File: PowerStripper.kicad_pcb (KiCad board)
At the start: 4 copper layers, 42.7 x 38.3 mm, 5 parts, among them J1 0548190519, J2 UE27AC54100

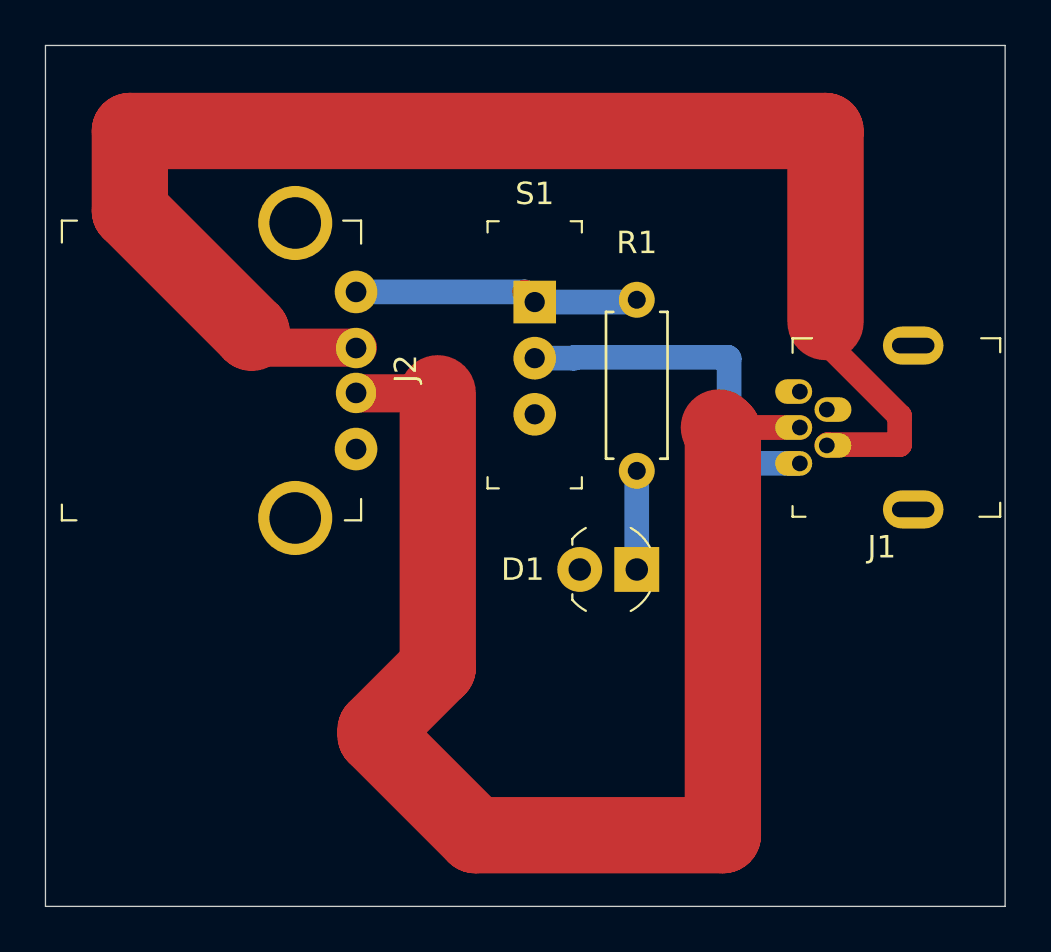
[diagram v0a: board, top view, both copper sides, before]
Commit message: finished making changes to make it compatible with jlcpcb
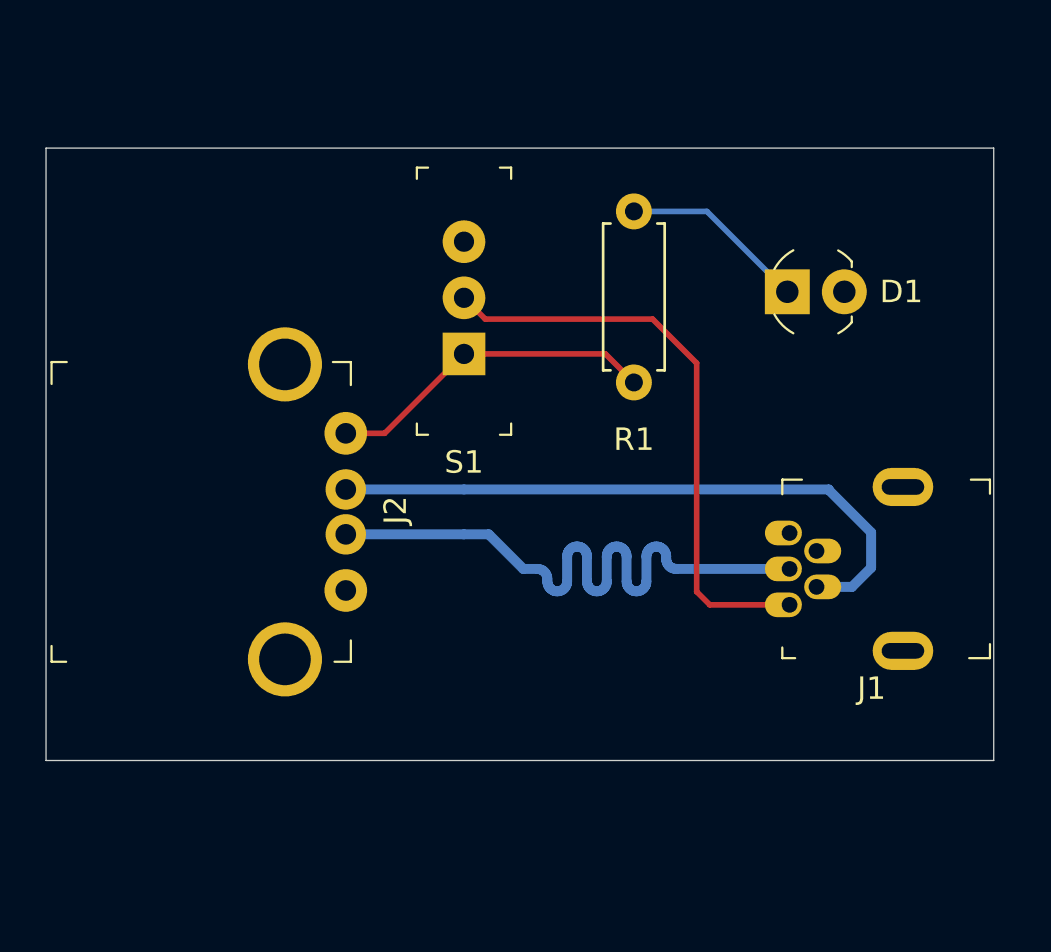
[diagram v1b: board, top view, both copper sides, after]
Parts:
- moved D1 17.1 mm to (128.1, 99.9), turned to 0 degrees
- moved R1 11.6 mm to (118.7, 96.3), turned to 270 degrees
- moved J1 6.32 mm to (125.7, 112.2)
- moved J2 6.32 mm to (103.2, 109.7)
- moved S1 3.91 mm to (111.2, 102.6), turned to 90 degrees
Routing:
- net D-: track 65.6 -> 28.6 mm
- net D+: track 59.3 -> 29.7 mm
- net Net-(J1-Pad1): track 16.5 -> 26.1 mm
- net Net-(D1-Pad1): track 4.39 -> 8.32 mm
- net Net-(J2-Pad1): track 13.5 -> 14.8 mm
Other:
- board size 42.7 x 38.3 mm -> 42.2 x 27.3 mm
- net class USB: trace_width 3.4 -> 0.441219
